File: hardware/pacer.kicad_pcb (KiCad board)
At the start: 2 copper layers, 88.2 x 78.1 mm, 38 parts, among them J1 Conn_01x04, J2 Conn_01x02_Pin, J3 Conn_01x02_Pin, J4 Conn_01x02_Socket, J5 Conn_01x02_Socket, SW1 SW_SPST, SW2 SW_SPDT, U1 CH32V003FxPx, U2 XCL103D333CR-G, U3 BU4210G-TR, U4 74HC595, U5 74HC595, U6 74HC595, Y1 Crystal_GND24

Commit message: PCB v1
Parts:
- removed BT1: Battery_Cell, Battery:BatteryHolder_Keystone_2460_1xAA
- removed D1, D2, D3, D4: LED, LED_SMD:LED_0603_1608Metric_Pad1.05x0.95mm_HandSolder
- removed H3, H4: MountingHole, MountingHole:MountingHole_2.2mm_M2
- removed J4, J5: Conn_01x02_Socket, Connector_PinSocket_2.54mm:PinSocket_1x02_P2.54mm_Vertical
- removed LS1: PKM13EPYH4000-A0, My_lib:buzzer_pkm13
- removed the SW1 at (155.1, 50.0)
- added BAR3: OSX05201-GGR1, My_lib:OSX05201-GGR1, F.Cu at (143.2, 100.0)
- added G***: LOGO, LOGO, B.Cu at (141.3, 90.3)
- added R3: 4.7k, Resistor_SMD:R_0603_1608Metric_Pad0.98x0.95mm_HandSolder, F.Cu at (147.6, 91.5)
- SW1: renamed from SW2; moved to B.Cu
- moved D5 16.7 mm to (100.6, 90.8), turned to -90 degrees
- moved R2 15.6 mm to (101.5, 87.6)
- moved U4 3.40 mm to (132.8, 109.2)
- moved RN6 3.35 mm to (143.2, 100.0)
- moved RN1 2.62 mm to (130.4, 100.0)
- moved J1 2.40 mm to (123.2, 89.6)
- moved J3 1.00 mm to (146.6, 109.7)
- moved J2 0.50 mm to (97.5, 87.7)
- moved C4 0.43 mm to (135.4, 88.0)
- moved Y1 0.35 mm to (136.0, 90.9)
- moved C5 0.27 mm to (136.0, 93.8)
- turned SW1 to 0 degrees
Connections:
- D5 pad 1: Net-(D5-K) -> BUZZER_DRV
- J2 pad 1: +BATT -> BUZZER_DRV
- R2 pad 1: Net-(SW2-C) -> Net-(SW1-A)
- R2 pad 2: Net-(D5-K) -> BUZZER_DRV
- SW1 pad 1: unconnected-(SW2-A-Pad1) -> Net-(SW1-A)
- SW1 pad 3: Net-(SW2-C) -> unconnected-(SW1-C-Pad3)
- U1 pad 1: unconnected-(U1-PD4-Pad1) -> BUZZER
- U1 pad 10: BUZZER -> unconnected-(U1-PC0-Pad10)
- U1 pad 13: ~{LED_OE} -> unconnected-(U1-PC3-Pad13)
- U1 pad 17: unconnected-(U1-PC7-Pad17) -> IND
- U4 pad 1: IND3 -> Net-(U4-QB)
- U4 pad 13: ~{LED_OE} -> GND
- U4 pad 15: IND4 -> Net-(U4-QA)
- U4 pad 2: IND2 -> Net-(U4-QC)
- U4 pad 3: IND1 -> Net-(U4-QD)
- U5 pad 13: ~{LED_OE} -> GND
- U6 pad 13: ~{LED_OE} -> GND
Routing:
- net GND: track 65.1 -> 159.8 mm, vias 23 -> 25
- net ~{LED_OE}: track 69.4 -> 0.00 mm, vias 2 -> 0
- net Net-(U4-QA): track 0.00 -> 22.0 mm, vias 0 -> 1
- net Net-(BT1-+): track 18.4 -> 0.00 mm
- net Net-(SW2-C): track 16.7 -> 0.00 mm, vias 1 -> 0
- net Net-(BT1--): track 15.1 -> 0.00 mm
- net Net-(U4-QD): track 0.00 -> 14.9 mm
- net IND1: track 14.2 -> 0.00 mm
- net Net-(U4-QC): track 0.00 -> 14.0 mm
- net Net-(U4-QB): track 0.00 -> 12.6 mm
- net IND2: track 9.85 -> 0.00 mm
- net Net-(D5-K): track 7.84 -> 0.00 mm
- net IND4: track 7.20 -> 0.00 mm
- net IND3: track 5.52 -> 0.00 mm
- net BUZZER_DRV: track 0.00 -> 4.74 mm
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- removed copper zone on B.Cu, net Net-(J5-Pin_1)
- removed copper zone on F.Cu, net Net-(J5-Pin_1)
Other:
- board size 88.2 x 78.1 mm -> 63.4 x 28.1 mm
- board text added: "3"
- board text added: "G"
- board text added: "Mute SW"
- board text added: "Pacer designed by object1037"
- board text added: "S"
- board text added: "~{R}"

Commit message: jlcpcb production files
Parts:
- R2: value 1k -> 1.2k
- R3: value 4.7k -> 5.6k
- RN6: value 4.7k -> 1k
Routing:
- net GND: track 159.8 -> 195.1 mm, vias 25 -> 31

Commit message: reroute xtal
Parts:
- moved C4 3.61 mm to (133.4, 91.0), turned to 90 degrees
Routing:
- net GND: track 195.1 -> 203.2 mm, vias 31 -> 33
- net Net-(U1-PA1): track 8.87 -> 7.53 mm
- net ~{RST}: track 13.8 -> 13.0 mm
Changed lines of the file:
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@@
 	(footprint "Capacitor_SMD:C_0603_1608Metric_Pad1.08x0.95mm_HandSolder"
 		(layer "F.Cu")
-		(at 135.4 87.99 180)
+		(at 133.4 91 90)
 		(descr "Capacitor SMD 0603 (1608 Metric), square (rectangular) end terminal, IPC-7351 nominal with elongated pad for handsoldering. (Body size source: IPC-SM-782 page 76, https://www.pcb-3d.com/wordpress/wp-content/uploads/ipc-sm-782a_amendment_1_and_2.pdf), generated with kicad-footprint-generator")
 		(tags "capacitor handsolder")
 		(property "Reference" "C4"
-			(at 0 -1.43 0)
+			(at 0 -1.43 90)
 			(layer "F.SilkS")
 			(hide yes)
@@
 		)
 		(property "Value" "30p"
-			(at 0 1.43 0)
+			(at 0 1.43 90)
 			(layer "F.Fab")
 			(effects
@@
 		)
 		(property "Datasheet" "~"
-			(at 0 0 0)
+			(at 0 0 90)
 			(layer "F.Fab")
 			(hide yes)
@@
 		)
 		(property "Description" "Unpolarized capacitor"
-			(at 0 0 0)
+			(at 0 0 90)
 			(layer "F.Fab")
 			(hide yes)
@@
 		)
 		(property "LCSC" "C1658"
-			(at 0 0 0)
+			(at 0 0 90)
 			(layer "F.SilkS")
 			(hide yes)
@@
 		(attr smd)
 		(fp_line
-			(start -0.146267 0.51)
-			(end 0.146267 0.51)
+			(start -0.146267 -0.51)
+			(end 0.146267 -0.51)
 			(stroke
 				(width 0.12)
@@
 		)
 		(fp_line
-			(start -0.146267 -0.51)
-			(end 0.146267 -0.51)
+			(start -0.146267 0.51)
+			(end 0.146267 0.51)
 			(stroke
 				(width 0.12)
@@
 		)
 		(fp_line
-			(start 1.65 0.73)
-			(end -1.65 0.73)
+			(start 1.65 -0.73)
+			(end 1.65 0.73)
 			(stroke
 				(width 0.05)
@@
 		)
 		(fp_line
-			(start 1.65 -0.73)
-			(end 1.65 0.73)
+			(start -1.65 -0.73)
+			(end 1.65 -0.73)
 			(stroke
 				(width 0.05)
@@
 		)
 		(fp_line
-			(start -1.65 0.73)
-			(end -1.65 -0.73)
+			(start 1.65 0.73)
+			(end -1.65 0.73)
 			(stroke
 				(width 0.05)
@@
 		)
 		(fp_line
-			(start -1.65 -0.73)
-			(end 1.65 -0.73)
+			(start -1.65 0.73)
+			(end -1.65 -0.73)
 			(stroke
 				(width 0.05)
@@
 		)
 		(fp_line
-			(start 0.8 0.4)
-			(end -0.8 0.4)
+			(start 0.8 -0.4)
+			(end 0.8 0.4)
 			(stroke
 				(width 0.1)
@@
 		)
 		(fp_line
-			(start 0.8 -0.4)
-			(end 0.8 0.4)
+			(start -0.8 -0.4)
+			(end 0.8 -0.4)
 			(stroke
 				(width 0.1)
@@
 		)
 		(fp_line
-			(start -0.8 0.4)
-			(end -0.8 -0.4)
+			(start 0.8 0.4)
+			(end -0.8 0.4)
 			(stroke
 				(width 0.1)
@@
 		)
 		(fp_line
-			(start -0.8 -0.4)
-			(end 0.8 -0.4)
+			(start -0.8 0.4)
+			(end -0.8 -0.4)
 			(stroke
 				(width 0.1)
@@
 		)
 		(fp_text user "${REFERENCE}"
-			(at 0 0 0)
+			(at 0 0 90)
 			(layer "F.Fab")
 			(effects
@@
 		)
 		(pad "1" smd roundrect
-			(at -0.8625 0 180)
+			(at -0.8625 0 90)
 			(size 1.075 0.95)
 			(layers "F.Cu" "F.Mask" "F.Paste")
@@
 		)
 		(pad "2" smd roundrect
-			(at 0.8625 0 180)
+			(at 0.8625 0 90)
 			(size 1.075 0.95)
 			(layers "F.Cu" "F.Mask" "F.Paste")
@@
 	)
 	(segment
-		(start 136.82 88.5475)
-		(end 136.2625 87.99)
-		(width 0.3)
-		(layer "F.Cu")
-		(net 21)
-	)
-	(segment
 		(start 138.6 91.4325)
 		(end 137.9863 91.4325)
@@
 	)
 	(segment
+		(start 134.9825 91.8625)
+		(end 135.12 92)
+		(width 0.3)
+		(layer "F.Cu")
+		(net 21)
+	)
+	(segment
 		(start 140.1375 90.775)
 		(end 139.2575 90.775)
@@
 	)
 	(segment
+		(start 133.4 91.8625)
+		(end 134.9825 91.8625)
+		(width 0.3)
+		(layer "F.Cu")
+		(net 21)
+	)
+	(segment
 		(start 133.435 110.565)
 		(end 134 110)
@@
 	)
 	(segment
-		(start 136.82 89.8)
-		(end 136.82 88.5475)
-		(width 0.3)
-		(layer "F.Cu")
-		(net 21)
-	)
-	(segment
 		(start 91.425 87.775)
 		(end 91.2 88)
@@
 	)
 	(via
+		(at 133.1 89)
+		(size 0.45)
+		(drill 0.3)
+		(layers "F.Cu" "B.Cu")
+		(free yes)
+		(net 21)
+	)
+	(via
 		(at 87 87.1)
 		(size 0.45)
@@
 	)
 	(via
+		(at 127.4 92.2)
+		(size 0.45)
+		(drill 0.3)
+		(layers "F.Cu" "B.Cu")
+		(free yes)
+		(net 21)
+	)
+	(via
 		(at 126.7 100.9)
 		(size 0.6)
@@
 	)
 	(segment
+		(start 137.601 88.601)
+		(end 138.1 89.1)
+		(width 0.3)
+		(layer "B.Cu")
+		(net 21)
+	)
+	(segment
 		(start 117.808 99.892)
 		(end 116.8 100.9)
@@
 	)
 	(segment
+		(start 133.3 89.6)
+		(end 134.299 88.601)
+		(width 0.3)
+		(layer "B.Cu")
+		(net 21)
+	)
+	(segment
 		(start 87.328 94.872)
 		(end 89.3 92.9)
@@
 	)
 	(segment
+		(start 134.299 88.601)
+		(end 137.601 88.601)
+		(width 0.3)
+		(layer "B.Cu")
+		(net 21)
+	)
+	(segment
 		(start 89.3 92.9)
 		(end 96.1 92.9)
@@
 	)
 	(segment
+		(start 138.1 89.1)
+		(end 138.1 89.5)
+		(width 0.3)
+		(layer "B.Cu")
+		(net 21)
+	)
+	(segment
 		(start 87.328 105.328)
 		(end 87.328 94.872)
@@
 	)
 	(segment
+		(start 130.81 89.6)
+		(end 133.3 89.6)
+		(width 0.3)
+		(layer "B.Cu")
+		(net 21)
+	)
+	(segment
 		(start 117.8 101.9)
 		(end 116.8 100.9)
@@
 	)
 	(segment
-		(start 135.2635 87.264)
-		(end 137.189001 87.264)
+		(start 138.92484 88.849)
+		(end 139.55084 89.475)
 		(width 0.2)
 		(layer "F.Cu")
@@
 	)
 	(segment
-		(start 134.5375 89.2175)
-		(end 135.12 89.8)
+		(start 139.55084 89.475)
+		(end 140.1375 89.475)
 		(width 0.2)
 		(layer "F.Cu")
@@
 	)
 	(segment
-		(start 137.189001 87.264)
-		(end 139.400001 89.475)
+		(start 133.7375 89.8)
+		(end 133.4 90.1375)
 		(width 0.2)
 		(layer "F.Cu")
@@
 	)
 	(segment
-		(start 134.5375 87.99)
-		(end 134.5375 89.2175)
+		(start 135.12 89.8)
+		(end 133.7375 89.8)
 		(width 0.2)
 		(layer "F.Cu")
@@
 	)
 	(segment
-		(start 139.400001 89.475)
-		(end 140.1375 89.475)
+		(start 136.071 88.849)
+		(end 138.92484 88.849)
 		(width 0.2)
 		(layer "F.Cu")
@@
 	)
 	(segment
-		(start 134.5375 87.99)
-		(end 135.2635 87.264)
+		(start 135.12 89.8)
+		(end 136.071 88.849)
 		(width 0.2)
 		(layer "F.Cu")
@@
 	)
 	(segment
-		(start 137.475001 86.9)
-		(end 139.400001 88.825)
-		(width 0.15)
+		(start 138.62584 87.9)
+		(end 139.55084 88.825)
+		(width 0.2)
 		(layer "F.Cu")
 		(net 36)
 	)
 	(segment
-		(start 139.400001 88.825)
-		(end 140.1375 88.825)
-		(width 0.15)
+		(start 129.97 87.9)
+		(end 138.62584 87.9)
+		(width 0.2)
 		(layer "F.Cu")
 		(net 36)
 	)
 	(segment
-		(start 128.27 89.6)
-		(end 130.97 86.9)
-		(width 0.15)
+		(start 139.55084 88.825)
+		(end 140.1375 88.825)
+		(width 0.2)
 		(layer "F.Cu")
 		(net 36)
 	)
 	(segment
-		(start 130.97 86.9)
-		(end 137.475001 86.9)
-		(width 0.15)
+		(start 128.27 89.6)
+		(end 129.97 87.9)
+		(width 0.2)
 		(layer "F.Cu")
 		(net 36)
@@
 	)
 	(segment
-		(start 105.8 87)
-		(end 108.4 87)
+		(start 123.688 86.9)
+		(end 140.1125 86.9)
 		(width 0.2)
 		(layer "F.Cu")
@@
 	)
 	(segment
-		(start 108.4 87)
-		(end 113.9 92.5)
+		(start 118.088 92.5)
+		(end 123.688 86.9)
 		(width 0.2)
 		(layer "F.Cu")
@@
 	)
 	(segment
-		(start 118.088 92.5)
-		(end 124.014 86.574)
+		(start 108.4 87)
+		(end 113.9 92.5)
 		(width 0.2)
 		(layer "F.Cu")
@@
 	)
 	(segment
-		(start 139.8365 86.574)
-		(end 140.1375 86.875)
+		(start 113.9 92.5)
+		(end 118.088 92.5)
 		(width 0.2)
 		(layer "F.Cu")
@@
 	)
 	(segment
-		(start 124.014 86.574)
-		(end 139.8365 86.574)
+		(start 105.8 87)
+		(end 108.4 87)
 		(width 0.2)
 		(layer "F.Cu")
@@
 	)
 	(segment
-		(start 113.9 92.5)
-		(end 118.088 92.5)
+		(start 140.1125 86.9)
+		(end 140.1375 86.875)
 		(width 0.2)
 		(layer "F.Cu")
@@
 			)
 		)
+	)
+	(zone
+		(net 0)
+		(net_name "")
+		(layers "F.Cu" "B.Cu")
+		(hatch edge 0.5)
+		(connect_pads
+			(clearance 0)
+		)
+		(min_thickness 0.25)
+		(filled_areas_thickness no)
+		(keepout
+			(tracks allowed)
+			(vias allowed)
+			(pads allowed)
+			(copperpour not_allowed)
+			(footprints allowed)
+		)
+		(placement
+			(enabled no)
+			(sheetname "")
+		)
+		(fill
+			(thermal_gap 0.5)
+			(thermal_bridge_width 0.5)
+		)
+		(polygon
+			(pts
+				(xy 134.1 88.7) (xy 137.8 88.7) (xy 137.8 93.1) (xy 134.1 93.1)
+			)
+		)

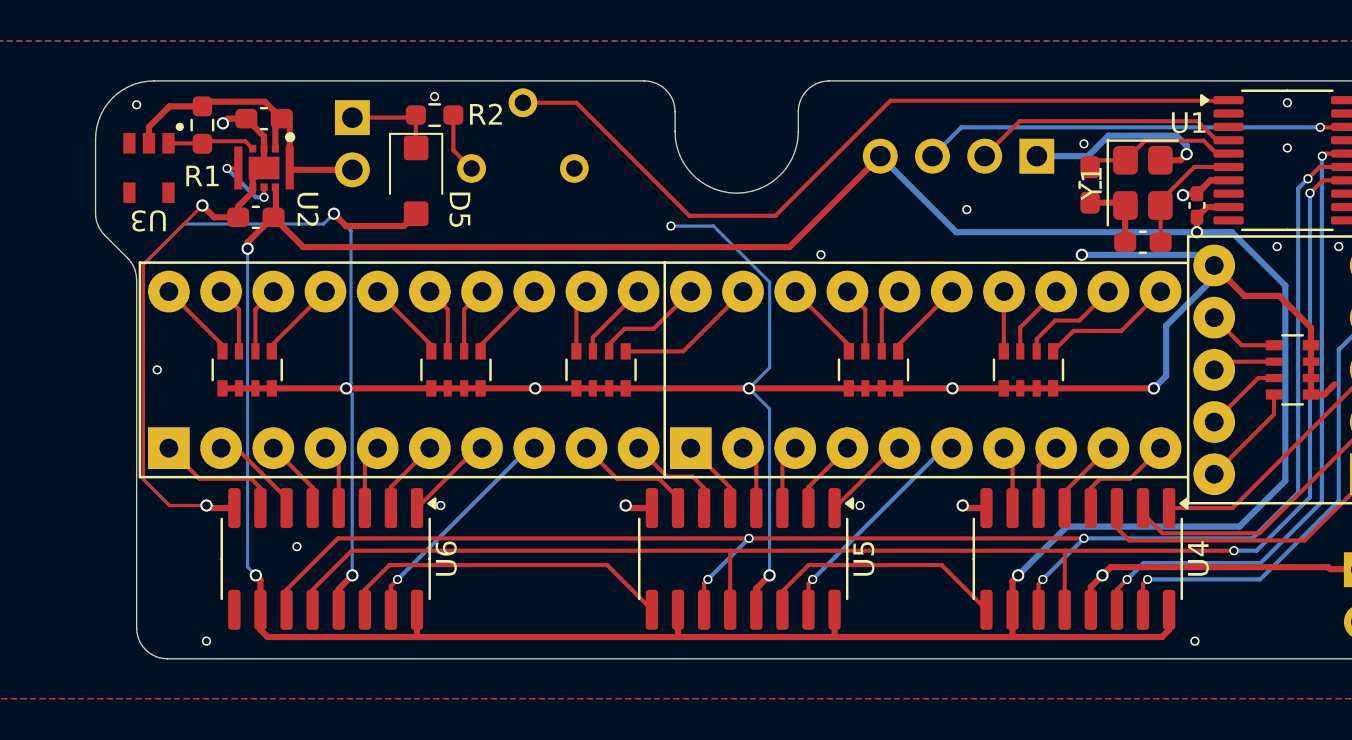
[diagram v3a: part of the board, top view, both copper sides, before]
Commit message: add capacitors
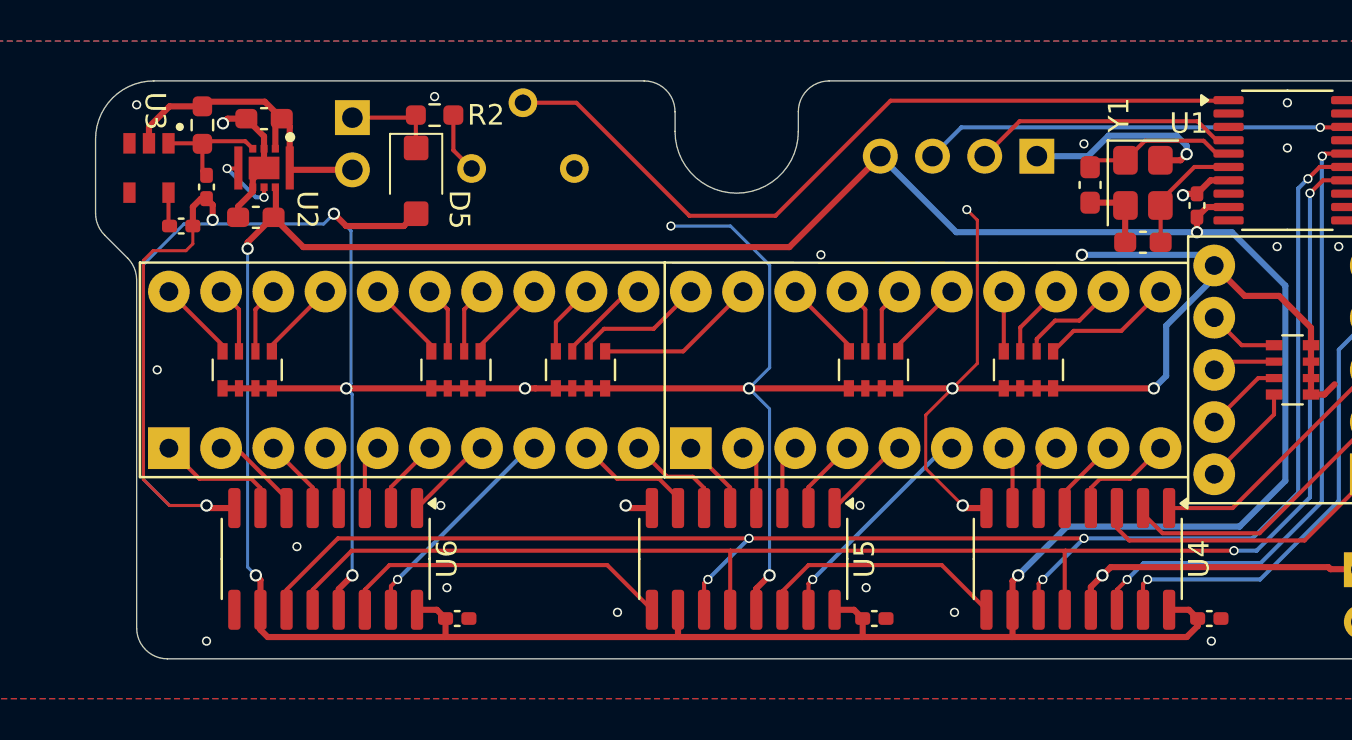
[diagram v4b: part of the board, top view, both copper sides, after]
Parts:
- added C10: 0.1u, Capacitor_SMD:C_0402_1005Metric_Pad0.74x0.62mm_HandSolder, F.Cu at (102.6, 112.1)
- added C6: 100p, Capacitor_SMD:C_0402_1005Metric_Pad0.74x0.62mm_HandSolder, F.Cu at (89.2, 93.0)
- added C7: 1n, Capacitor_SMD:C_0402_1005Metric_Pad0.74x0.62mm_HandSolder, F.Cu at (90.4, 91.1)
- added C8: 0.1u, Capacitor_SMD:C_0402_1005Metric_Pad0.74x0.62mm_HandSolder, F.Cu at (139.2, 112.1)
- added C9: 0.1u, Capacitor_SMD:C_0402_1005Metric_Pad0.74x0.62mm_HandSolder, F.Cu at (122.9, 112.1)
- moved RN3 1.00 mm to (108.6, 100.0)
- turned U3 to -90 degrees
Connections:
- U3 pad 5: unconnected-(U3-CT-Pad5) -> Net-(U3-CT)
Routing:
- net GND: track 203.2 -> 220.7 mm, vias 33 -> 37
- net +3V3: track 156.2 -> 160.9 mm
- net Net-(U3-CT): track 0.00 -> 1.65 mm
- net Net-(U2-CE): track 4.31 -> 5.93 mm
- net Net-(RN3-R4.2): track 6.92 -> 7.92 mm
- net Net-(RN3-R3.2): track 5.38 -> 6.38 mm
- net Net-(RN3-R2.2): track 3.83 -> 4.55 mm

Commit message: update silkscreen
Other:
- board text removed: "Mute SW"
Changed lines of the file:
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@@
 			)
 		)
-		(property "LCSC" "C1525"
-			(at 0 0 0)
-			(layer "F.SilkS")
-			(hide yes)
-			(effects
-				(font
-					(size 1.27 1.27)
-					(thickness 0.15)
-				)
-			)
-		)
 		(property ki_fp_filters "C_*")
 		(sheetname "/")
@@
 			)
 		)
-		(property "LCSC" "C1525"
-			(at 0 0 0)
-			(layer "F.SilkS")
-			(hide yes)
-			(effects
-				(font
-					(size 1.27 1.27)
-					(thickness 0.15)
-				)
-			)
-		)
 		(property ki_fp_filters "C_*")
 		(sheetname "/")
@@
 			)
 		)
-		(property "LCSC" "C1525"
-			(at 0 0 0)
-			(layer "F.SilkS")
-			(hide yes)
-			(effects
-				(font
-					(size 1.27 1.27)
-					(thickness 0.15)
-				)
-			)
-		)
 		(property ki_fp_filters "C_*")
 		(sheetname "/")
@@
 		)
 	)
-	(gr_text "Mute SW"
-		(at 110.4 93 0)
-		(layer "B.SilkS")
-		(effects
-			(font
-				(size 1 1)
-				(thickness 0.153)
-			)
-			(justify left bottom mirror)
-		)
-	)
